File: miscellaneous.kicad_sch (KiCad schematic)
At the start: 4 parts, among them SW7001 SW_MEC_5E, SW7002 SW_MEC_5E, SW7003 SW_MEC_5E, SW7004 SW_MEC_5E

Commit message: Small clean up
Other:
- note added: "Buttons"
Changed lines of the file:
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@@
 	(generator_version "9.0")
 	(paper "A3")
+	(text "Buttons"
+		(exclude_from_sim no)
+		(at 252.476 27.686 0)
+		(effects
+			(font
+				(size 6.35 6.35)
+				(thickness 1.27)
+				(bold yes)
+			)
+		)
+	)
 	(junction
 		(at 320.04 54.61)

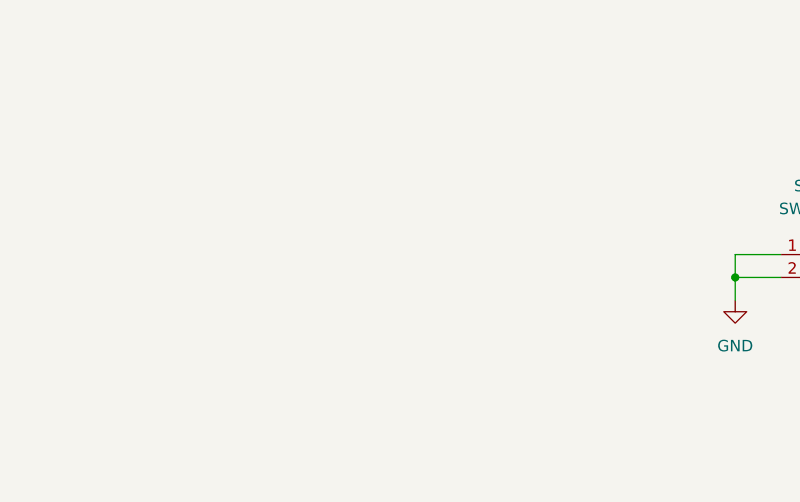
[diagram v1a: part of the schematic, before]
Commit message: Added status LEDs for SoC power, MGM240P power, and for GPIO0_70
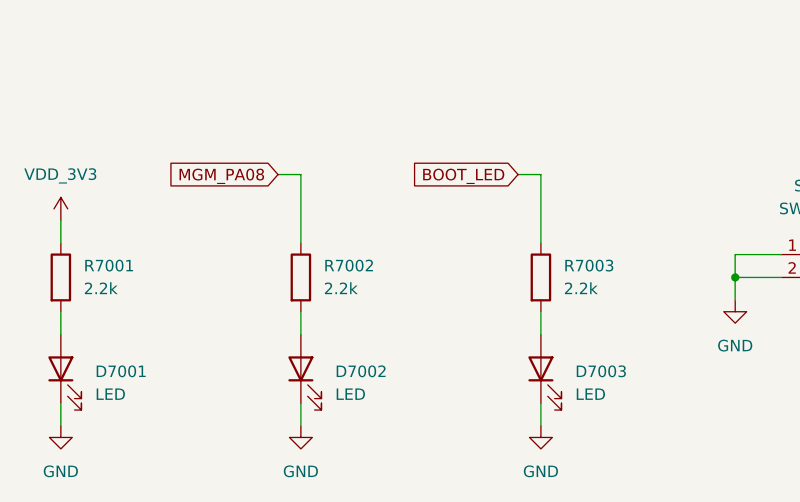
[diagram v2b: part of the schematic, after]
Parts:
- added D7001, D7002, D7003: LED, LED_SMD:LED_0402_1005Metric, symbol Device:LED
- added R7001, R7002, R7003: 2.2k, Resistor_SMD:R_0402_1005Metric, symbol Device:R
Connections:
- net GND: now also D7001.1 (K), D7002.1 (K), D7003.1 (K)
- new net: D7001.2 (A), R7001.2
- new net: D7003.2 (A), R7003.2
- new net: D7002.2 (A), R7002.2
- new net BOOT_LED: R7003.1
- new net MGM_PA08: R7002.1
- new net VDD_3V3: R7001.1

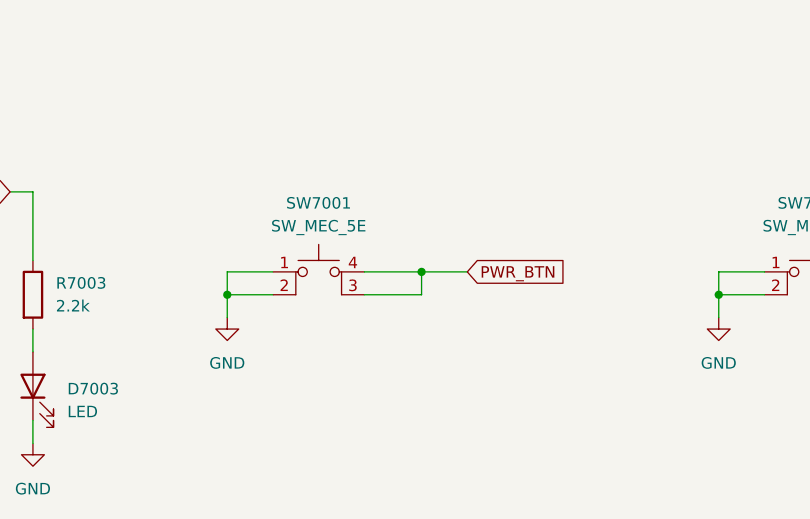
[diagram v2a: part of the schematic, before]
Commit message: Added JLCPCB part numbers for some caps
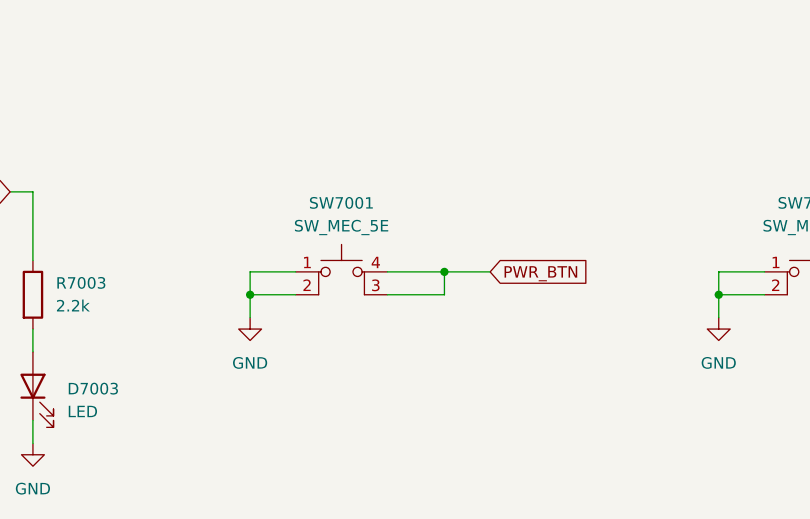
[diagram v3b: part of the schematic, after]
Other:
- moved on the sheet: SW7001
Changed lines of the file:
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@@
 	)
 	(junction
-		(at 151.13 54.61)
+		(at 153.67 54.61)
 		(diameter 0)
 		(color 0 0 0 0)
@@
 	)
 	(junction
-		(at 172.72 52.07)
+		(at 175.26 52.07)
 		(diameter 0)
 		(color 0 0 0 0)
@@
 	(wire
 		(pts
-			(xy 151.13 54.61) (xy 151.13 57.15)
+			(xy 153.67 54.61) (xy 153.67 57.15)
 		)
 		(stroke
@@
 	(wire
 		(pts
-			(xy 172.72 54.61) (xy 172.72 52.07)
+			(xy 175.26 54.61) (xy 175.26 52.07)
 		)
 		(stroke
@@
 	(wire
 		(pts
-			(xy 166.37 54.61) (xy 172.72 54.61)
+			(xy 168.91 54.61) (xy 175.26 54.61)
 		)
 		(stroke
@@
 	(wire
 		(pts
-			(xy 156.21 52.07) (xy 151.13 52.07)
+			(xy 158.75 52.07) (xy 153.67 52.07)
 		)
 		(stroke
@@
 	(wire
 		(pts
-			(xy 172.72 52.07) (xy 177.8 52.07)
+			(xy 175.26 52.07) (xy 180.34 52.07)
 		)
 		(stroke
@@
 	(wire
 		(pts
-			(xy 151.13 54.61) (xy 156.21 54.61)
+			(xy 153.67 54.61) (xy 158.75 54.61)
 		)
 		(stroke
@@
 	(wire
 		(pts
-			(xy 151.13 52.07) (xy 151.13 54.61)
-		)
-		(stroke
-			(width 0)
-			(type default)
-		)
-	)
-	(wire
-		(pts
-			(xy 166.37 52.07) (xy 172.72 52.07)
+			(xy 153.67 52.07) (xy 153.67 54.61)
+		)
+		(stroke
+			(width 0)
+			(type default)
+		)
+	)
+	(wire
+		(pts
+			(xy 168.91 52.07) (xy 175.26 52.07)
 		)
 		(stroke
@@
 	(global_label "PWR_BTN"
 		(shape input)
-		(at 177.8 52.07 0)
+		(at 180.34 52.07 0)
 		(fields_autoplaced yes)
 		(effects
@@
 		)
 		(property "Intersheetrefs" "${INTERSHEET_REFS}"
-			(at 189.3123 52.07 0)
+			(at 191.8523 52.07 0)
 			(effects
 				(font
@@
 			)
 		)
+		(property "JLCPCB Part#" ""
+			(at 270.51 54.61 0)
+			(effects
+				(font
+					(size 1.27 1.27)
+				)
+			)
+		)
 		(pin "1"
 		)
@@
 			)
 		)
+		(property "JLCPCB Part#" ""
+			(at 76.2 54.61 0)
+			(effects
+				(font
+					(size 1.27 1.27)
+				)
+			)
+		)
 		(pin "2"
 		)
@@
 			)
 		)
+		(property "JLCPCB Part#" ""
+			(at 331.47 54.61 0)
+			(effects
+				(font
+					(size 1.27 1.27)
+				)
+			)
+		)
 		(pin "1"
 		)
@@
 			)
 		)
+		(property "JLCPCB Part#" ""
+			(at 129.54 64.77 0)
+			(effects
+				(font
+					(size 1.27 1.27)
+				)
+			)
+		)
 		(pin "1"
 		)
@@
 			)
 		)
+		(property "JLCPCB Part#" ""
+			(at 102.87 64.77 0)
+			(effects
+				(font
+					(size 1.27 1.27)
+				)
+			)
+		)
 		(pin "1"
 		)
@@
 			)
 		)
+		(property "JLCPCB Part#" ""
+			(at 129.54 54.61 0)
+			(effects
+				(font
+					(size 1.27 1.27)
+				)
+			)
+		)
 		(pin "2"
 		)
@@
 			)
 		)
+		(property "JLCPCB Part#" ""
+			(at 215.9 54.61 0)
+			(effects
+				(font
+					(size 1.27 1.27)
+				)
+			)
+		)
 		(pin "1"
 		)
@@
 	(symbol
 		(lib_id "power:GND")
-		(at 151.13 57.15 0)
+		(at 153.67 57.15 0)
 		(unit 1)
 		(exclude_from_sim no)
@@
 		(fields_autoplaced yes)
 		(property "Reference" "#PWR07001"
-			(at 151.13 63.5 0)
+			(at 153.67 63.5 0)
 			(effects
 				(font
@@
 		)
 		(property "Value" "GND"
-			(at 151.13 62.23 0)
+			(at 153.67 62.23 0)
 			(effects
 				(font
@@
 		)
 		(property "Footprint" ""
-			(at 151.13 57.15 0)
+			(at 153.67 57.15 0)
 			(effects
 				(font
@@
 		)
 		(property "Datasheet" ""
-			(at 151.13 57.15 0)
+			(at 153.67 57.15 0)
 			(effects
 				(font
@@
 		)
 		(property "Description" "Power symbol creates a global label with name \"GND\" , ground"
-			(at 151.13 57.15 0)
+			(at 153.67 57.15 0)
 			(effects
 				(font
@@
 			)
 		)
+		(property "JLCPCB Part#" ""
+			(at 76.2 64.77 0)
+			(effects
+				(font
+					(size 1.27 1.27)
+				)
+			)
+		)
 		(pin "1"
 		)
@@
 	(symbol
 		(lib_id "Switch:SW_MEC_5E")
-		(at 161.29 54.61 0)
+		(at 163.83 54.61 0)
 		(unit 1)
 		(exclude_from_sim no)
@@
 		(fields_autoplaced yes)
 		(property "Reference" "SW7001"
-			(at 161.29 44.45 0)
+			(at 163.83 44.45 0)
 			(effects
 				(font
@@
 		)
 		(property "Value" "SW_MEC_5E"
-			(at 161.29 46.99 0)
+			(at 163.83 46.99 0)
 			(effects
 				(font
@@
 		)
 		(property "Footprint" "SoftServicesFootprintLibrary:1825910-6"
-			(at 161.29 46.99 0)
+			(at 163.83 46.99 0)
 			(effects
 				(font
@@
 		)
 		(property "Datasheet" "http://www.apem.com/int/index.php?controller=attachment&id_attachment=1371"
-			(at 161.29 46.99 0)
+			(at 163.83 46.99 0)
 			(effects
 				(font
@@
 		)
 		(property "Description" "MEC 5E single pole normally-open tactile switch"
-			(at 161.29 54.61 0)
-			(effects
-				(font
-					(size 1.27 1.27)
-				)
-				(hide yes)
+			(at 163.83 54.61 0)
+			(effects
+				(font
+					(size 1.27 1.27)
+				)
+				(hide yes)
+			)
+		)
+		(property "JLCPCB Part#" ""
+			(at 163.83 54.61 0)
+			(effects
+				(font
+					(size 1.27 1.27)
+				)
 			)
 		)
@@
 			)
 		)
+		(property "JLCPCB Part#" ""
+			(at 102.87 54.61 0)
+			(effects
+				(font
+					(size 1.27 1.27)
+				)
+			)
+		)

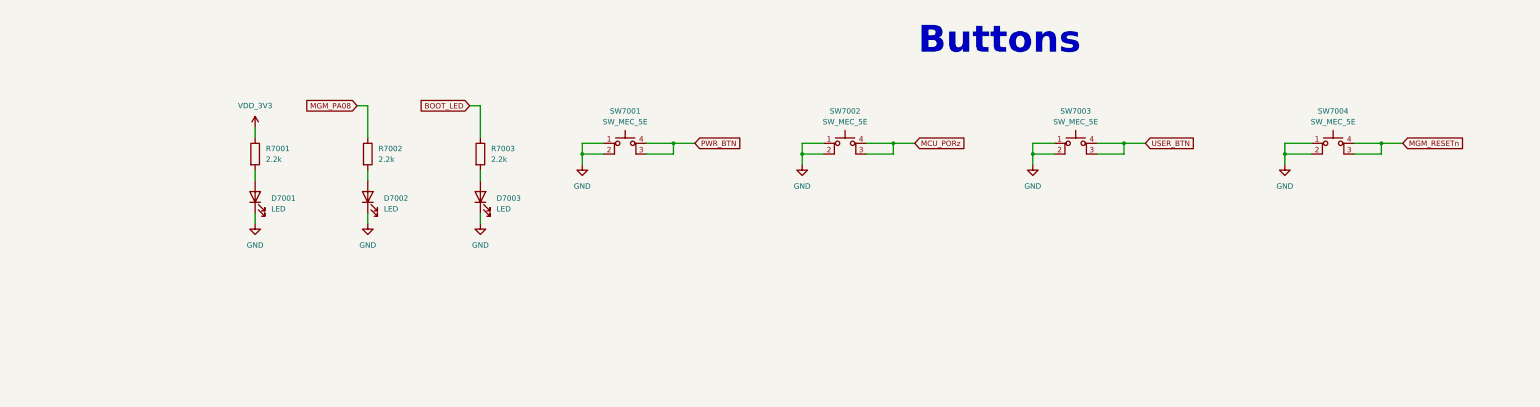
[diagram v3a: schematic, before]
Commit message: All JLC part numbers added to BOM except LEDs
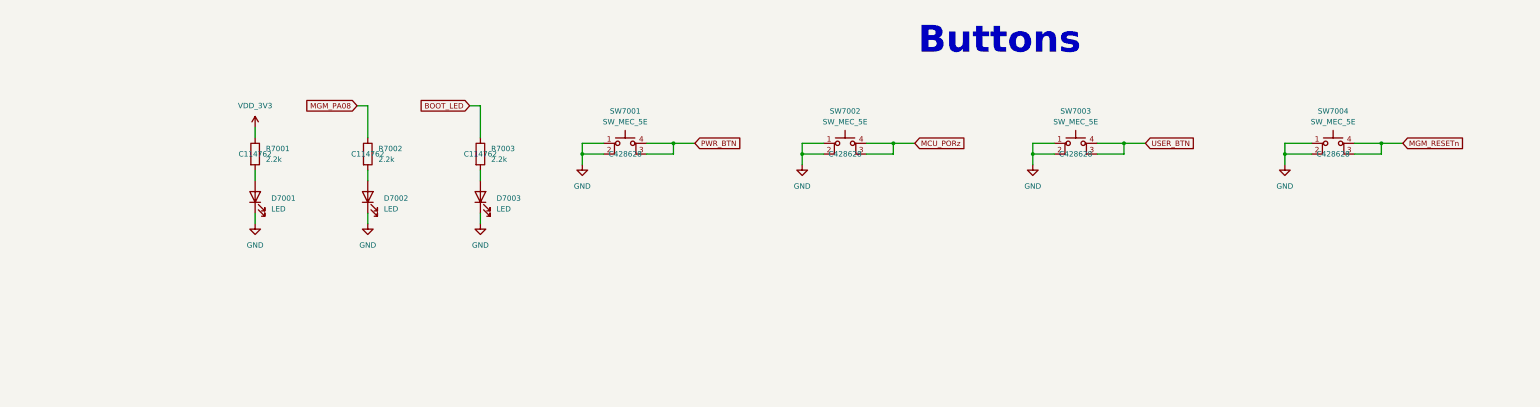
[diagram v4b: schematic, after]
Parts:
- R7001, R7002, R7003: JLCPCB Part# (none) -> C114762
- SW7001, SW7002, SW7003, SW7004: JLCPCB Part# (none) -> C428628
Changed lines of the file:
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@@
 			)
 		)
-		(property "JLCPCB Part#" ""
+		(property "JLCPCB Part#" "C428628"
 			(at 270.51 54.61 0)
 			(effects
@@
 			)
 		)
-		(property "JLCPCB Part#" ""
+		(property "JLCPCB Part#" "C114762"
 			(at 76.2 54.61 0)
 			(effects
@@
 			)
 		)
-		(property "JLCPCB Part#" ""
+		(property "JLCPCB Part#" "C428628"
 			(at 331.47 54.61 0)
 			(effects
@@
 			)
 		)
-		(property "JLCPCB Part#" ""
+		(property "JLCPCB Part#" "C114762"
 			(at 129.54 54.61 0)
 			(effects
@@
 			)
 		)
-		(property "JLCPCB Part#" ""
+		(property "JLCPCB Part#" "C428628"
 			(at 215.9 54.61 0)
 			(effects
@@
 			)
 		)
-		(property "JLCPCB Part#" ""
+		(property "JLCPCB Part#" "C428628"
 			(at 163.83 54.61 0)
 			(effects
@@
 			)
 		)
-		(property "JLCPCB Part#" ""
+		(property "JLCPCB Part#" "C114762"
 			(at 102.87 54.61 0)
 			(effects

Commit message: Finished adding JLC part numbers to BOM
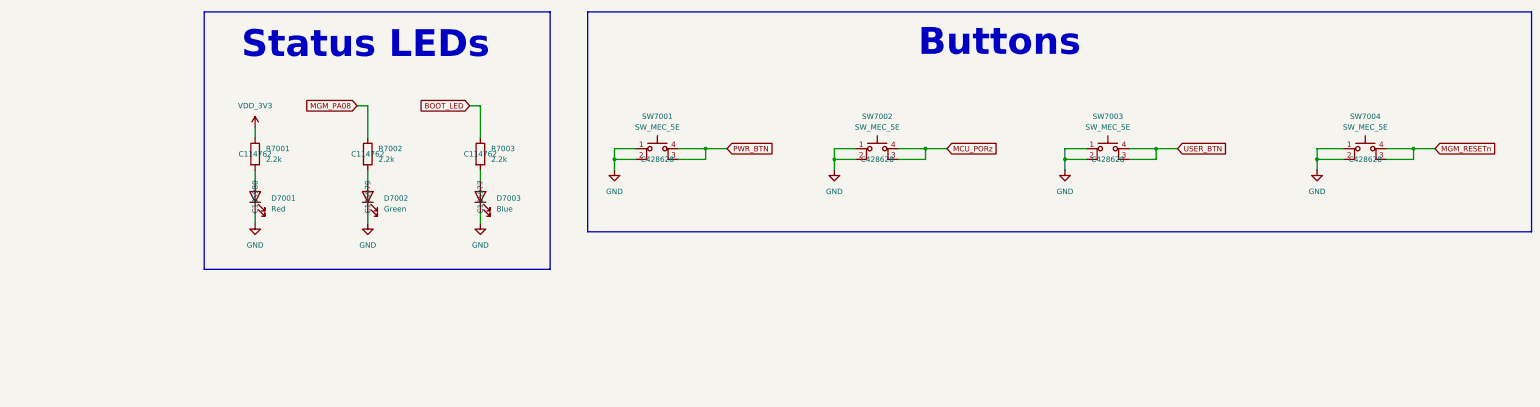
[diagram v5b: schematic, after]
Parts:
- D7001: value LED -> Red; JLCPCB Part# (none) -> C165980
- D7002: value LED -> Green; JLCPCB Part# (none) -> C165979
- D7003: value LED -> Blue; JLCPCB Part# (none) -> C165977
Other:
- note added: "Status LEDs"
- moved on the sheet: SW7001, SW7002, SW7003, SW7004

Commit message: Small DDR4 cleanup
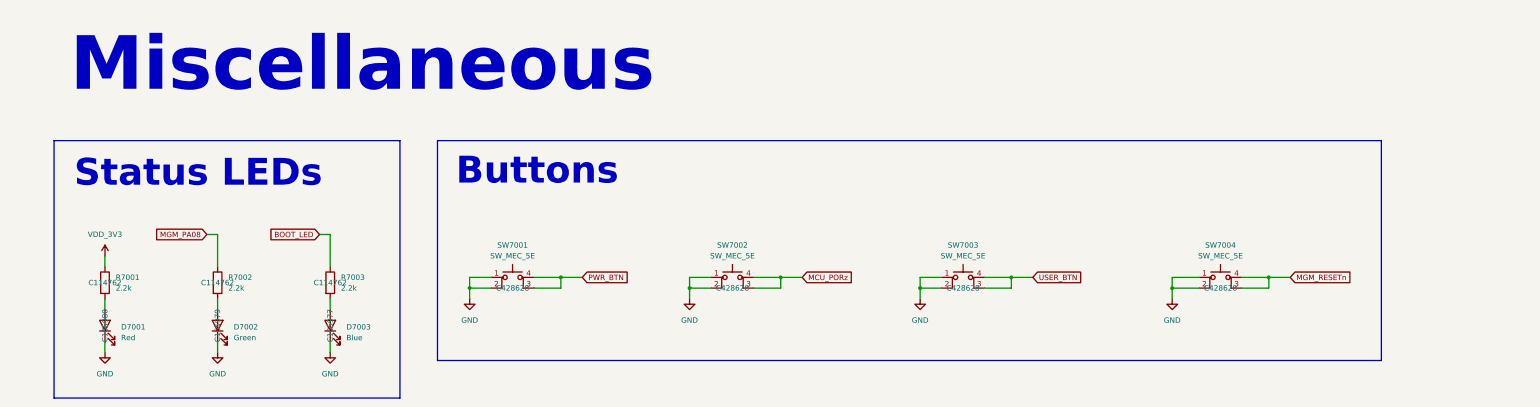
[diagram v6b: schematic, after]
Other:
- note added: "Miscellaneous"
- moved on the sheet: D7001, D7002, D7003, R7001, R7002, R7003, SW7001, SW7002, SW7003, SW7004
